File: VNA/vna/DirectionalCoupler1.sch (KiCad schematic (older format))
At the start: 6 parts

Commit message: adjusted main schematic to suit initial presentation
i moved a few blocks around so that the cropped version of the block diagram would fit nicely in my semester 1 presentation
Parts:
- renumbered L3 to L2, L2 to L3
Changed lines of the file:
@@
 k1 l5 l6 0.999
 $Comp
-L Device:L L2
+L Device:L L3
 U 1 1 5CC2B8A8
 P 5000 3300
-AR Path="/5CC1CC6B/5CC2B8A8" Ref="L2"  Part="1"
-AR Path="/5CC2F156/5CC2B8A8" Ref="L6"  Part="1"
+AR Path="/5CC1CC6B/5CC2B8A8" Ref="L3"  Part="1"
+AR Path="/5CC2F156/5CC2B8A8" Ref="L?"  Part="1"
 AR Path="/5CC6A089/5CC2B8A8" Ref="L?"  Part="1"
-F 0 "L2" V 4950 3200 50  0000 C CNN
+F 0 "L3" V 4950 3200 50  0000 C CNN
 F 1 "L" V 4950 3400 50  0000 C CNN
 F 2 "" H 5000 3300 50  0001 C CNN
@@
 P 5800 3500
 AR Path="/5CC1CC6B/5CC2B8AE" Ref="L4"  Part="1"
-AR Path="/5CC2F156/5CC2B8AE" Ref="L8"  Part="1"
+AR Path="/5CC2F156/5CC2B8AE" Ref="L?"  Part="1"
 AR Path="/5CC6A089/5CC2B8AE" Ref="L?"  Part="1"
 F 0 "L4" V 5850 3350 50  0000 C CNN
@@
 	5650 3300 5650 3500
 $Comp
-L power:GND #PWR04
+L power:GND #PWR03
 U 1 1 5CC2B8B8
 P 5950 3250
-AR Path="/5CC1CC6B/5CC2B8B8" Ref="#PWR04"  Part="1"
-AR Path="/5CC2F156/5CC2B8B8" Ref="#PWR07"  Part="1"
+AR Path="/5CC1CC6B/5CC2B8B8" Ref="#PWR03"  Part="1"
+AR Path="/5CC2F156/5CC2B8B8" Ref="#PWR?"  Part="1"
 AR Path="/5CC6A089/5CC2B8B8" Ref="#PWR?"  Part="1"
-F 0 "#PWR04" H 5950 3000 50  0001 C CNN
+F 0 "#PWR03" H 5950 3000 50  0001 C CNN
 F 1 "GND" H 6050 3150 50  0000 C CNN
 F 2 "" H 5950 3250 50  0001 C CNN
@@
 P 5950 3700
 AR Path="/5CC1CC6B/5CC2B8BE" Ref="R2"  Part="1"
-AR Path="/5CC2F156/5CC2B8BE" Ref="R4"  Part="1"
+AR Path="/5CC2F156/5CC2B8BE" Ref="R?"  Part="1"
 AR Path="/5CC6A089/5CC2B8BE" Ref="R?"  Part="1"
 F 0 "R2" H 6018 3746 50  0000 L CNN
@@
 P 4850 3500
 AR Path="/5CC1CC6B/5CC70FE9" Ref="R1"  Part="1"
-AR Path="/5CC2F156/5CC70FE9" Ref="R3"  Part="1"
+AR Path="/5CC2F156/5CC70FE9" Ref="R?"  Part="1"
 AR Path="/5CC6A089/5CC70FE9" Ref="R?"  Part="1"
 F 0 "R1" H 4918 3546 50  0000 L CNN
@@
 Connection ~ 5950 3500
 $Comp
-L power:GND #PWR03
+L power:GND #PWR04
 U 1 1 5CC70FEA
 P 4850 3600
-AR Path="/5CC1CC6B/5CC70FEA" Ref="#PWR03"  Part="1"
-AR Path="/5CC2F156/5CC70FEA" Ref="#PWR06"  Part="1"
+AR Path="/5CC1CC6B/5CC70FEA" Ref="#PWR04"  Part="1"
+AR Path="/5CC2F156/5CC70FEA" Ref="#PWR?"  Part="1"
 AR Path="/5CC6A089/5CC70FEA" Ref="#PWR?"  Part="1"
-F 0 "#PWR03" H 4850 3350 50  0001 C CNN
+F 0 "#PWR04" H 4850 3350 50  0001 C CNN
 F 1 "GND" H 4950 3500 50  0000 C CNN
 F 2 "" H 4850 3600 50  0001 C CNN
@@
 P 5950 3800
 AR Path="/5CC1CC6B/5CC70FEB" Ref="#PWR05"  Part="1"
-AR Path="/5CC2F156/5CC70FEB" Ref="#PWR08"  Part="1"
+AR Path="/5CC2F156/5CC70FEB" Ref="#PWR?"  Part="1"
 AR Path="/5CC6A089/5CC70FEB" Ref="#PWR?"  Part="1"
 F 0 "#PWR05" H 5950 3550 50  0001 C CNN
@@
 P 5000 3050
 AR Path="/5CC1CC6B/5CC70FEC" Ref="L1"  Part="1"
-AR Path="/5CC2F156/5CC70FEC" Ref="L5"  Part="1"
+AR Path="/5CC2F156/5CC70FEC" Ref="L?"  Part="1"
 AR Path="/5CC6A089/5CC70FEC" Ref="L?"  Part="1"
 F 0 "L1" V 4950 2950 50  0000 C CNN
@@
 $EndComp
 $Comp
-L Device:L L3
+L Device:L L2
 U 1 1 5CC70FED
 P 5800 3250
-AR Path="/5CC1CC6B/5CC70FED" Ref="L3"  Part="1"
-AR Path="/5CC2F156/5CC70FED" Ref="L7"  Part="1"
+AR Path="/5CC1CC6B/5CC70FED" Ref="L2"  Part="1"
+AR Path="/5CC2F156/5CC70FED" Ref="L?"  Part="1"
 AR Path="/5CC6A089/5CC70FED" Ref="L?"  Part="1"
-F 0 "L3" V 5750 3150 50  0000 C CNN
+F 0 "L2" V 5750 3150 50  0000 C CNN
 F 1 "L" V 5750 3400 50  0000 C CNN
 F 2 "" H 5800 3250 50  0001 C CNN

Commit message: changed inductors to a single transformer component
inductors in the directional couplers was changed to a single transformer

this will help with later layout opperations
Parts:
- removed L1, L2, L3, L4: L, symbol Device:L
- removed R1, R2: 50, symbol Device:R_Small_US
- added R? (x2): 50, symbol Device:R_Small_US
- added T? (x2): Transformer_1P_1S, symbol Device:Transformer_1P_1S
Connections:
- wire segments 12 -> 16
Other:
- note added: "Pins 1 and 2 of transformer are the coaxial cable, pins 3 and 4 the smaller wire that is wrapped around the toroid.\n\nThe transformer should be wound as a 1:10 ratio"
- note removed: "k1 l3 l4 0.999"
- note removed: "k1 l5 l6 0.999"

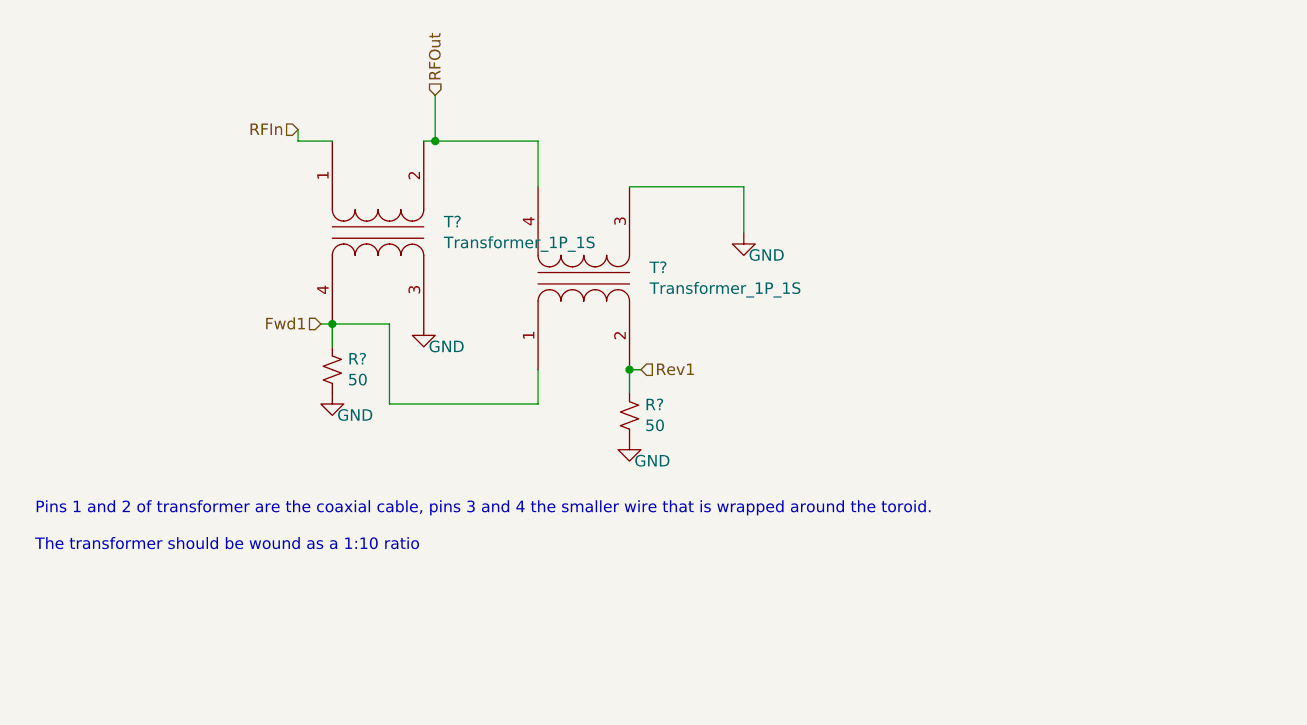
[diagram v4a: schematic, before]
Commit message: micro-controller pins labelled
micro controller pins have been labelled, the pins on the bottom are yet to be linked to them.

still to wire up ftdi chip,

still to decide upon rf switch control schema.
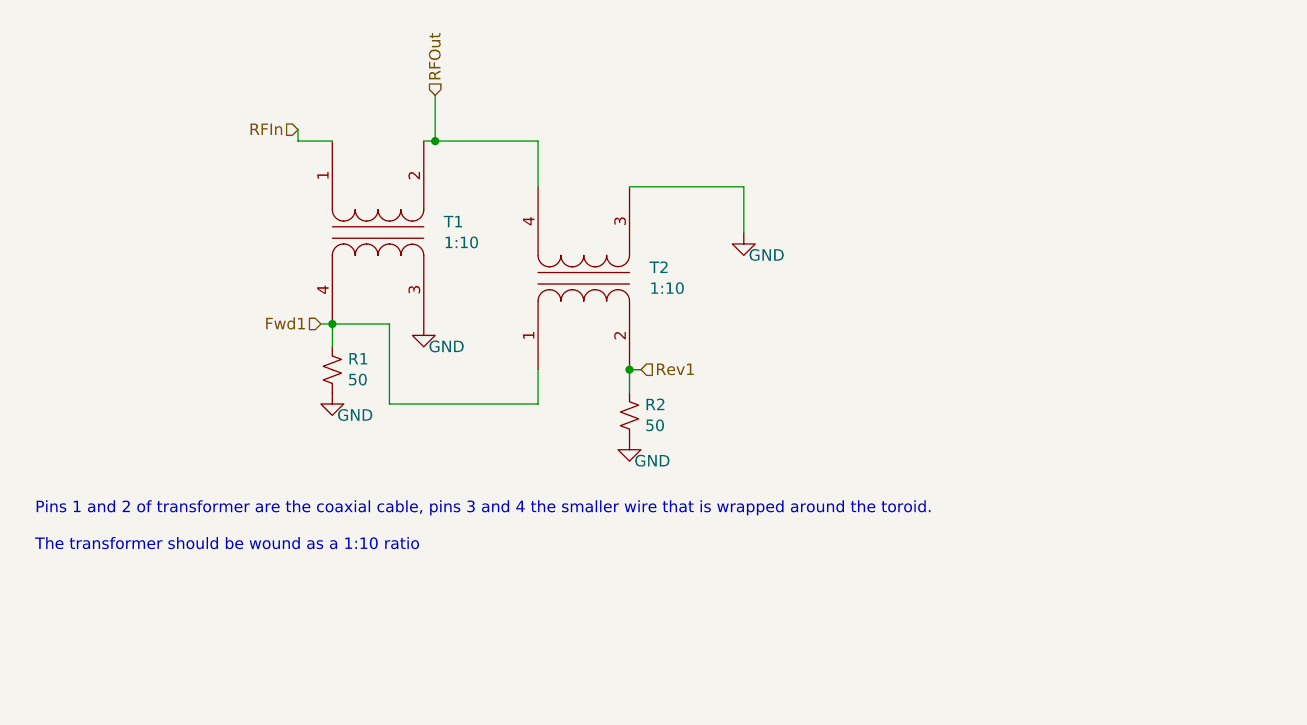
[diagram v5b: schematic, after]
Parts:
- T1, T2: renamed from T?; value Transformer_1P_1S -> 1:10
- gave numbers to parts that had none: 2
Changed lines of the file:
@@
 	6550 2300 6550 2500
 $Comp
-L power:GND #PWR?
+L power:GND #PWR03
 U 1 1 5CF4AF9A
 P 6550 2500
-AR Path="/5CC1CC6B/5CF4AF9A" Ref="#PWR?"  Part="1"
+AR Path="/5CC1CC6B/5CF4AF9A" Ref="#PWR03"  Part="1"
 AR Path="/5CC2F156/5CF4AF9A" Ref="#PWR?"  Part="1"
 AR Path="/5CC6A089/5CF4AF9A" Ref="#PWR?"  Part="1"
-F 0 "#PWR?" H 6550 2250 50  0001 C CNN
+F 0 "#PWR03" H 6550 2250 50  0001 C CNN
 F 1 "GND" H 6650 2400 50  0000 C CNN
 F 2 "" H 6550 2500 50  0001 C CNN
@@
 $EndComp
 $Comp
-L Device:R_Small_US R?
+L Device:R_Small_US R2
 U 1 1 5CF4AFA0
 P 6050 3300
-AR Path="/5CC1CC6B/5CF4AFA0" Ref="R?"  Part="1"
+AR Path="/5CC1CC6B/5CF4AFA0" Ref="R2"  Part="1"
 AR Path="/5CC2F156/5CF4AFA0" Ref="R?"  Part="1"
 AR Path="/5CC6A089/5CF4AFA0" Ref="R?"  Part="1"
-F 0 "R?" H 6118 3346 50  0000 L CNN
+F 0 "R2" H 6118 3346 50  0000 L CNN
 F 1 "50" H 6118 3255 50  0000 L CNN
 F 2 "" H 6050 3300 50  0001 C CNN
@@
 $EndComp
 $Comp
-L Device:R_Small_US R?
+L Device:R_Small_US R1
 U 1 1 5CF4AFA6
 P 4750 3100
-AR Path="/5CC1CC6B/5CF4AFA6" Ref="R?"  Part="1"
+AR Path="/5CC1CC6B/5CF4AFA6" Ref="R1"  Part="1"
 AR Path="/5CC2F156/5CF4AFA6" Ref="R?"  Part="1"
 AR Path="/5CC6A089/5CF4AFA6" Ref="R?"  Part="1"
-F 0 "R?" H 4818 3146 50  0000 L CNN
+F 0 "R1" H 4818 3146 50  0000 L CNN
 F 1 "50" H 4818 3055 50  0000 L CNN
 F 2 "" H 4750 3100 50  0001 C CNN
@@
 	6050 3200 6050 3100
 $Comp
-L power:GND #PWR?
+L power:GND #PWR05
 U 1 1 5CF4AFB0
 P 4750 3200
-AR Path="/5CC1CC6B/5CF4AFB0" Ref="#PWR?"  Part="1"
+AR Path="/5CC1CC6B/5CF4AFB0" Ref="#PWR05"  Part="1"
 AR Path="/5CC2F156/5CF4AFB0" Ref="#PWR?"  Part="1"
 AR Path="/5CC6A089/5CF4AFB0" Ref="#PWR?"  Part="1"
-F 0 "#PWR?" H 4750 2950 50  0001 C CNN
+F 0 "#PWR05" H 4750 2950 50  0001 C CNN
 F 1 "GND" H 4850 3100 50  0000 C CNN
 F 2 "" H 4750 3200 50  0001 C CNN
@@
 $EndComp
 $Comp
-L power:GND #PWR?
+L power:GND #PWR06
 U 1 1 5CF4AFB6
 P 6050 3400
-AR Path="/5CC1CC6B/5CF4AFB6" Ref="#PWR?"  Part="1"
+AR Path="/5CC1CC6B/5CF4AFB6" Ref="#PWR06"  Part="1"
 AR Path="/5CC2F156/5CF4AFB6" Ref="#PWR?"  Part="1"
 AR Path="/5CC6A089/5CF4AFB6" Ref="#PWR?"  Part="1"
-F 0 "#PWR?" H 6050 3150 50  0001 C CNN
+F 0 "#PWR06" H 6050 3150 50  0001 C CNN
 F 1 "GND" H 6150 3300 50  0000 C CNN
 F 2 "" H 6050 3400 50  0001 C CNN
@@
 RFIn
 $Comp
-L Device:Transformer_1P_1S T?
+L Device:Transformer_1P_1S T1
 U 1 1 5CF4AFC7
 P 4950 2500
-F 0 "T?" V 4904 2212 50  0000 R CNN
-F 1 "Transformer_1P_1S" V 4995 2212 50  0000 R CNN
+F 0 "T1" V 4904 2212 50  0000 R CNN
+F 1 "1:10" V 4995 2212 50  0000 R CNN
 F 2 "" H 4950 2500 50  0001 C CNN
 F 3 "~" H 4950 2500 50  0001 C CNN
@@
 $EndComp
 $Comp
-L Device:Transformer_1P_1S T?
+L Device:Transformer_1P_1S T2
 U 1 1 5CF4AFCD
 P 5850 2700
-F 0 "T?" V 5896 2412 50  0000 R CNN
-F 1 "Transformer_1P_1S" V 5805 2412 50  0000 R CNN
+F 0 "T2" V 5896 2412 50  0000 R CNN
+F 1 "1:10" V 5805 2412 50  0000 R CNN
 F 2 "" H 5850 2700 50  0001 C CNN
 F 3 "~" H 5850 2700 50  0001 C CNN
@@
 	5650 3250 5650 3100
 $Comp
-L power:GND #PWR?
+L power:GND #PWR04
 U 1 1 5CF4AFD9
 P 5150 2900
-AR Path="/5CC1CC6B/5CF4AFD9" Ref="#PWR?"  Part="1"
+AR Path="/5CC1CC6B/5CF4AFD9" Ref="#PWR04"  Part="1"
 AR Path="/5CC2F156/5CF4AFD9" Ref="#PWR?"  Part="1"
 AR Path="/5CC6A089/5CF4AFD9" Ref="#PWR?"  Part="1"
-F 0 "#PWR?" H 5150 2650 50  0001 C CNN
+F 0 "#PWR04" H 5150 2650 50  0001 C CNN
 F 1 "GND" H 5250 2800 50  0000 C CNN
 F 2 "" H 5150 2900 50  0001 C CNN

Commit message: finished controller, chose compatible switches
controller and rf switches have been completed.

ToDo: finish filter design for RF Source, add auto gain control
ToDo: finish directional coupler footprints
ToDo: PCB Layout
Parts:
- R1, R2: footprint (none) -> Resistor_SMD:R_0805_2012Metric_Pad1.15x1.40mm_HandSolder
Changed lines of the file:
@@
 	6550 2300 6550 2500
 $Comp
-L power:GND #PWR03
+L power:GND #PWR08
 U 1 1 5CF4AF9A
 P 6550 2500
-AR Path="/5CC1CC6B/5CF4AF9A" Ref="#PWR03"  Part="1"
+AR Path="/5CC1CC6B/5CF4AF9A" Ref="#PWR08"  Part="1"
 AR Path="/5CC2F156/5CF4AF9A" Ref="#PWR?"  Part="1"
 AR Path="/5CC6A089/5CF4AF9A" Ref="#PWR?"  Part="1"
-F 0 "#PWR03" H 6550 2250 50  0001 C CNN
+F 0 "#PWR08" H 6550 2250 50  0001 C CNN
 F 1 "GND" H 6650 2400 50  0000 C CNN
 F 2 "" H 6550 2500 50  0001 C CNN
@@
 F 0 "R2" H 6118 3346 50  0000 L CNN
 F 1 "50" H 6118 3255 50  0000 L CNN
-F 2 "" H 6050 3300 50  0001 C CNN
+F 2 "Resistor_SMD:R_0805_2012Metric_Pad1.15x1.40mm_HandSolder" H 6050 3300 50  0001 C CNN
 F 3 "~" H 6050 3300 50  0001 C CNN
 	1    6050 3300
@@
 F 0 "R1" H 4818 3146 50  0000 L CNN
 F 1 "50" H 4818 3055 50  0000 L CNN
-F 2 "" H 4750 3100 50  0001 C CNN
+F 2 "Resistor_SMD:R_0805_2012Metric_Pad1.15x1.40mm_HandSolder" H 4750 3100 50  0001 C CNN
 F 3 "~" H 4750 3100 50  0001 C CNN
 	1    4750 3100
@@
 	6050 3200 6050 3100
 $Comp
-L power:GND #PWR05
+L power:GND #PWR010
 U 1 1 5CF4AFB0
 P 4750 3200
-AR Path="/5CC1CC6B/5CF4AFB0" Ref="#PWR05"  Part="1"
+AR Path="/5CC1CC6B/5CF4AFB0" Ref="#PWR010"  Part="1"
 AR Path="/5CC2F156/5CF4AFB0" Ref="#PWR?"  Part="1"
 AR Path="/5CC6A089/5CF4AFB0" Ref="#PWR?"  Part="1"
-F 0 "#PWR05" H 4750 2950 50  0001 C CNN
+F 0 "#PWR010" H 4750 2950 50  0001 C CNN
 F 1 "GND" H 4850 3100 50  0000 C CNN
 F 2 "" H 4750 3200 50  0001 C CNN
@@
 $EndComp
 $Comp
-L power:GND #PWR06
+L power:GND #PWR011
 U 1 1 5CF4AFB6
 P 6050 3400
-AR Path="/5CC1CC6B/5CF4AFB6" Ref="#PWR06"  Part="1"
+AR Path="/5CC1CC6B/5CF4AFB6" Ref="#PWR011"  Part="1"
 AR Path="/5CC2F156/5CF4AFB6" Ref="#PWR?"  Part="1"
 AR Path="/5CC6A089/5CF4AFB6" Ref="#PWR?"  Part="1"
-F 0 "#PWR06" H 6050 3150 50  0001 C CNN
+F 0 "#PWR011" H 6050 3150 50  0001 C CNN
 F 1 "GND" H 6150 3300 50  0000 C CNN
 F 2 "" H 6050 3400 50  0001 C CNN
@@
 	5650 3250 5650 3100
 $Comp
-L power:GND #PWR04
+L power:GND #PWR09
 U 1 1 5CF4AFD9
 P 5150 2900
-AR Path="/5CC1CC6B/5CF4AFD9" Ref="#PWR04"  Part="1"
+AR Path="/5CC1CC6B/5CF4AFD9" Ref="#PWR09"  Part="1"
 AR Path="/5CC2F156/5CF4AFD9" Ref="#PWR?"  Part="1"
 AR Path="/5CC6A089/5CF4AFD9" Ref="#PWR?"  Part="1"
-F 0 "#PWR04" H 5150 2650 50  0001 C CNN
+F 0 "#PWR09" H 5150 2650 50  0001 C CNN
 F 1 "GND" H 5250 2800 50  0000 C CNN
 F 2 "" H 5150 2900 50  0001 C CNN
